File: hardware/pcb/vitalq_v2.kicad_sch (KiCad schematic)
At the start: 302 parts, among them J1 USB-C, J10 Optical tail pads, J11 Sweat site, J12 FH12-14S, J13 MX ECG pads, J2 LiPo pads, J3 FSR pads, J5 ECG pads, J6 EDA pads, J7 Chest bioZ, J8 TC2030, J9 I2C tail pads, Q1 CSD13380F3T, Q2 CSD13380F3T, Q3 BC847BS,115, Q4 CSD13380F3T, Q6 AO3401A, SW1 TS-1088, SW2 TS-1088, U1 ESP32-S3-MINI-1-N4R2, U10 AS7341-DLGM, U11 TMP117AIDRVR, U12 MLX90632SLD-DCB-100-SP, U13 BME280, U14 LSM6DSV80XTR, U15 TPS61240YFFR, U16 SFH 7072, U17 MAX17048G+T10, U18 W25Q512JVEIQ, U19 TCA6408ARSVR, U2 BQ25170DSGR, U20 TMP117AIDRVR, U21 USBLC6-2SC6, U22 MAX86141ENP+, U23 SHT45-AD1B, U24 RV-3028-C7, U25 IM69D130, U26 SN74AXC2T245RSWR, U3 TPS63802DLAR, U4 TPS7A2018PDBVR, U5 CP2102N-A02-GQFN28R, U6 AFE4900YZR, U7 AD5940BCBZ-RL7, U8 ADS1292RIRSMT, U9 PCA9306DCUR

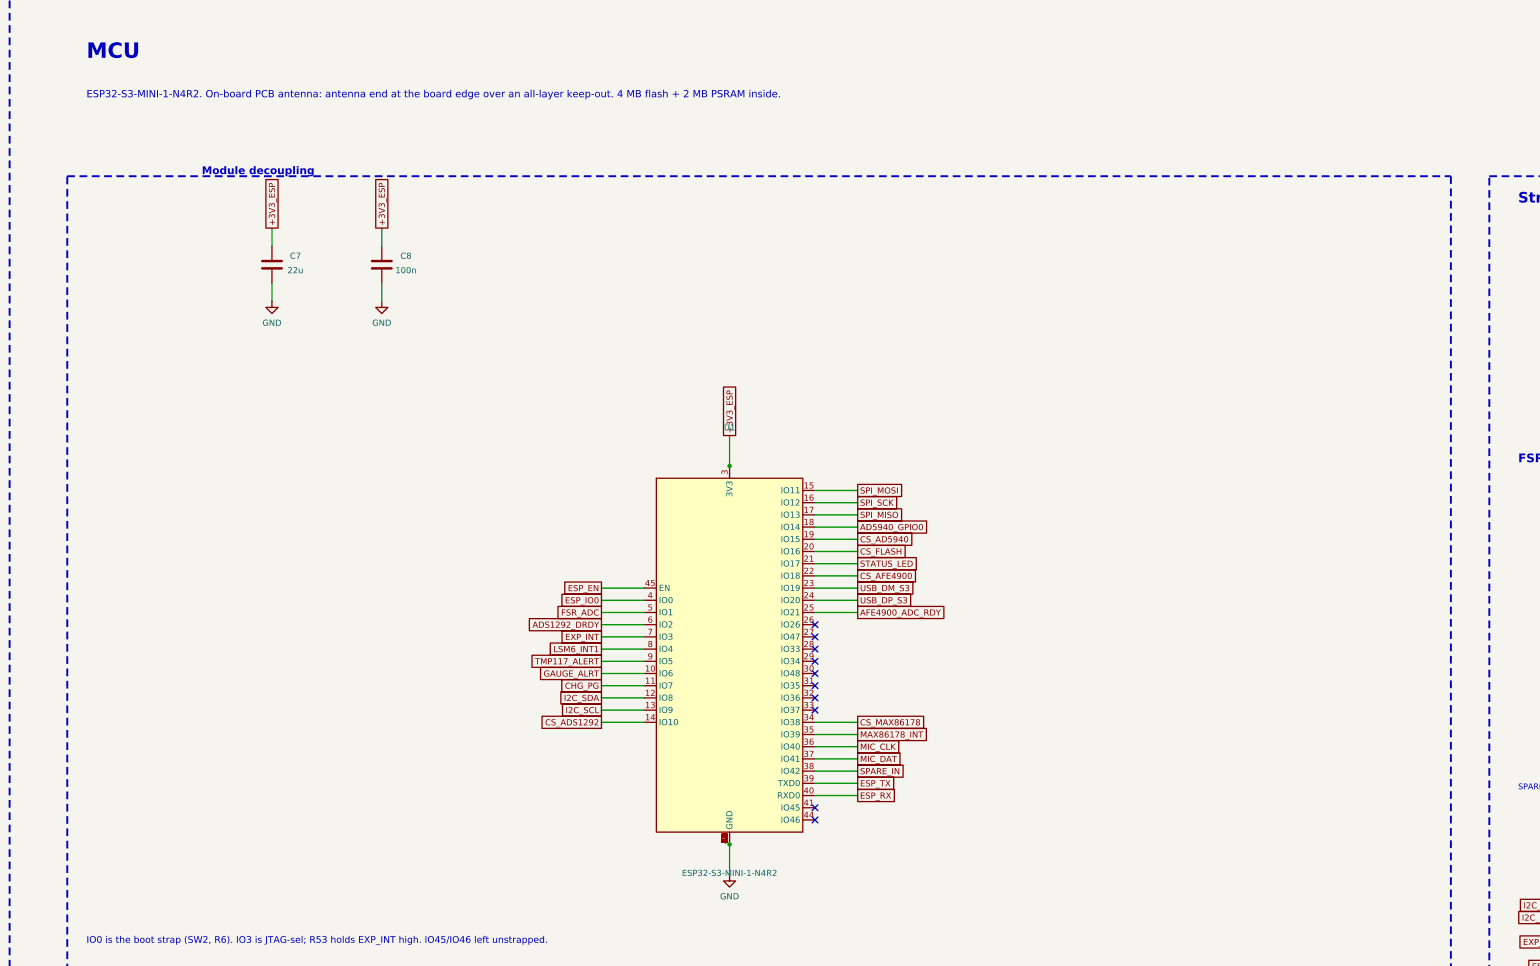
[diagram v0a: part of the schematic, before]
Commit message: hardware: swap pcb tree to verified fix_v22 board (J1 east move)
Move USB-C receptacle J1 from (26.0,-7.8) to (29.5,-7.8) rot 180 so a
real 12.4 mm cable overmould clears the WROOM tab/body. R2, TP11, TP20,
R26 minimally relocated; only CS_ADS1292/ESP_TX/SPARE_IN/GND re-routed
near the new J1 shield/courtyard. Schematic carries the WROOM-1-N16R8
module correction.

Verification: DRC 0 errors / 0 unconnected / 0 schematic parity, ERC 0,
12.4 mm and 8.3 mm grip corridors clear (0.80/1.66 mm margins), antenna
keep-outs empty, J1 pad nets verified on board + gerbers, full
component-vs-datasheet connection audit (CONNECTION_AUDIT_V22.md) — all
parts pass; one order note: MLX90632 must be the 1.8V I2C variant.

Fab: gerbers, drill (917 PTH / 8 NPTH), BOM/CPL (J1 = C165948,
29.5,7.8,Top,180), zip SHA-256 43ef4a31bf3880ad...267f. Reports:
V22_PROGRESS.md, VERIFY_REPORT.md, CASE_CHANGES_FOR_V22.md.

Generated with [Devin](https://devin.ai)

Co-Authored-By: Devin <158243242+devin-ai-integration[bot]@users.noreply.github.com>
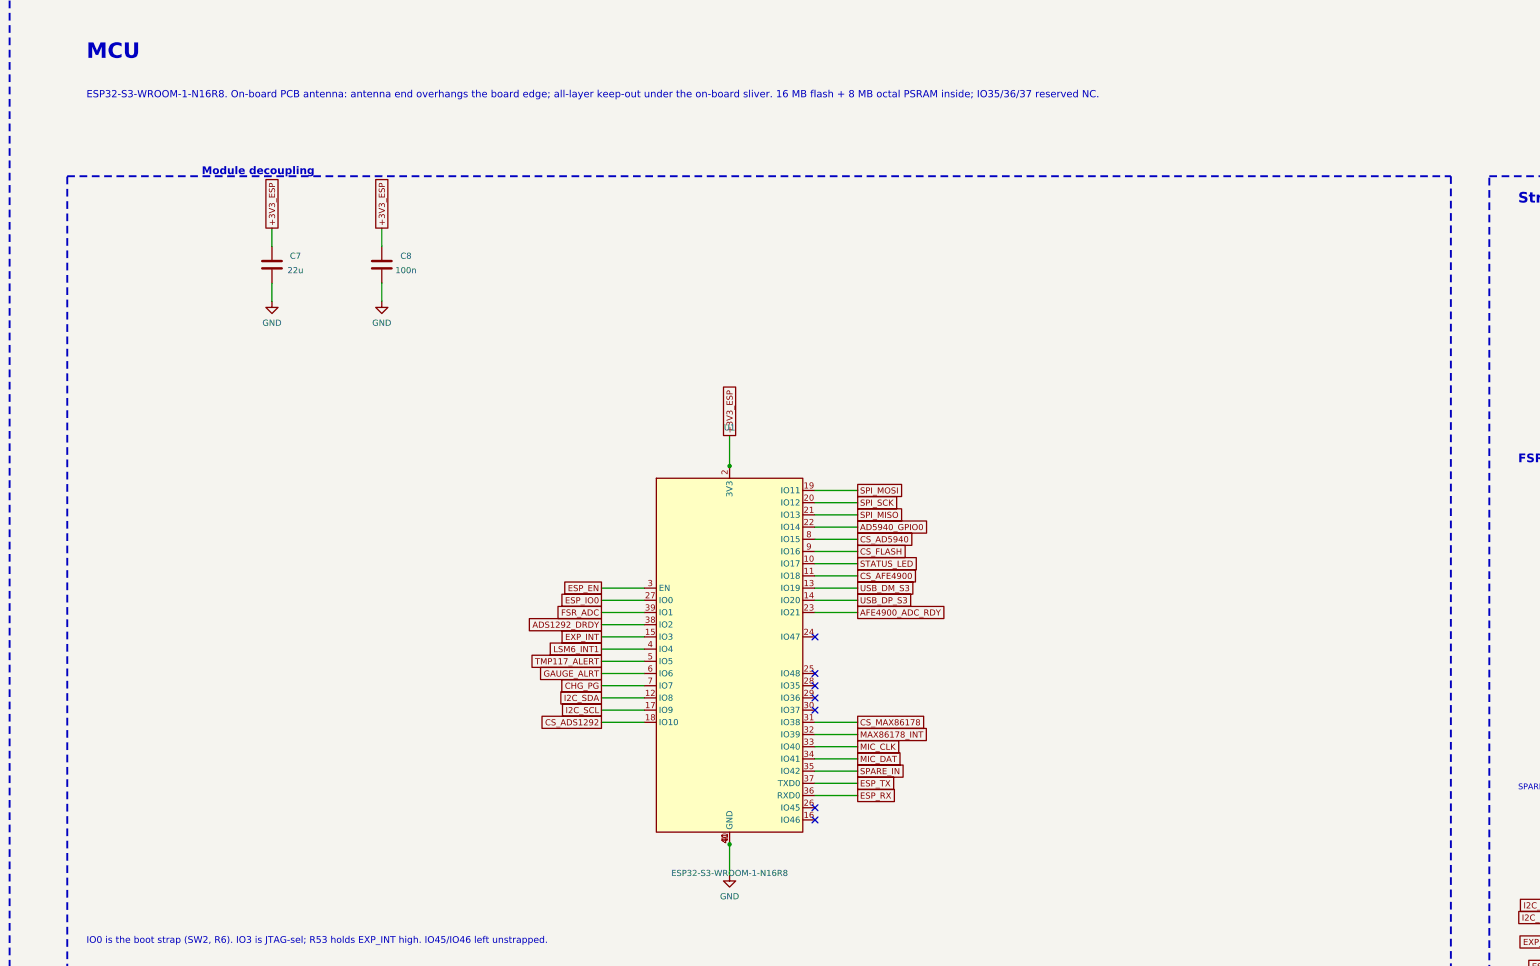
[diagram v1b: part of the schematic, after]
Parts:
- U1: value ESP32-S3-MINI-1-N4R2 -> ESP32-S3-WROOM-1-N16R8; footprint vitalq:ESP32_S3_MINI_1 -> vitalq:ESP32_S3_WROOM_1; symbol vitalq:ESP32-S3-MINI-1-N4R2 -> vitalq:ESP32-S3-WROOM-1-N16R8
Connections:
- net +3V3_ESP: now also U1.2 (3V3); no longer U1.3 (3V3)
- net AD5940_GPIO0: now also U1.22 (IO14); no longer U1.18 (IO14)
- net ADS1292_DRDY: now also U1.38 (IO2); no longer U1.6 (IO2)
- net AFE4900_ADC_RDY: now also U1.23 (IO21); no longer U1.25 (IO21)
- net CHG_PG: now also U1.7 (IO7); no longer U1.11 (IO7)
- net CS_AD5940: now also U1.8 (IO15); no longer U1.19 (IO15)
- net CS_ADS1292: now also U1.18 (IO10); no longer U1.14 (IO10)
- net CS_AFE4900: now also U1.11 (IO18); no longer U1.22 (IO18)
- net CS_FLASH: now also U1.9 (IO16); no longer U1.20 (IO16)
- net CS_MAX86178: now also U1.31 (IO38); no longer U1.34 (IO38)
- net ESP_EN: now also U1.3 (EN); no longer U1.45 (EN)
- net ESP_IO0: now also U1.27 (IO0); no longer U1.4 (IO0)
- net ESP_RX: now also U1.36 (RXD0); no longer U1.40 (RXD0)
- net ESP_TX: now also U1.37 (TXD0); no longer U1.39 (TXD0)
- net EXP_INT: now also U1.15 (IO3); no longer U1.7 (IO3)
- net FSR_ADC: now also U1.39 (IO1); no longer U1.5 (IO1)
- net GAUGE_ALRT: now also U1.6 (IO6); no longer U1.10 (IO6)
- net GND: now also U1.40 (GND), U1.41 (GND); no longer U1.2 (GND), U1.42 (GND), U1.43 (GND), U1.46 (GND), U1.47 (GND), U1.48 (GND), U1.49 (GND), U1.50 (GND), U1.51 (GND), U1.52 (GND), U1.53 (GND), U1.54 (GND), U1.55 (GND), U1.56 (GND), U1.57 (GND), U1.58 (GND), U1.59 (GND), U1.60 (GND), U1.61 (GND), U1.62 (GND), U1.63 (GND), U1.64 (GND), U1.65 (GND)
- net I2C_SCL: now also U1.17 (IO9); no longer U1.13 (IO9)
- net LSM6_INT1: now also U1.4 (IO4); no longer U1.8 (IO4)
- net MAX86178_INT: now also U1.32 (IO39); no longer U1.35 (IO39)
- net MIC_CLK: now also U1.33 (IO40); no longer U1.36 (IO40)
- net MIC_DAT: now also U1.34 (IO41); no longer U1.37 (IO41)
- net SPARE_IN: now also U1.35 (IO42); no longer U1.38 (IO42)
- net SPI_MISO: now also U1.21 (IO13); no longer U1.17 (IO13)
- net SPI_MOSI: now also U1.19 (IO11); no longer U1.15 (IO11)
- net SPI_SCK: now also U1.20 (IO12); no longer U1.16 (IO12)
- net STATUS_LED: now also U1.10 (IO17); no longer U1.21 (IO17)
- net TMP117_ALERT: now also U1.5 (IO5); no longer U1.9 (IO5)
- net USB_DM_S3: now also U1.13 (IO19); no longer U1.23 (IO19)
- net USB_DP_S3: now also U1.14 (IO20); no longer U1.24 (IO20)
- no-connect marks 57 -> 54
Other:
- note added: "ESP32-S3-WROOM-1-N16R8. On-board PCB antenna: antenna end overhangs the board edge; all-layer keep-out under the on-board sliver. 16 MB flash + 8 MB octal PSRAM inside; IO35/36/37 reserved NC."
- note removed: "ESP32-S3-MINI-1-N4R2. On-board PCB antenna: antenna end at the board edge over an all-layer keep-out. 4 MB flash + 2 MB PSRAM inside."
